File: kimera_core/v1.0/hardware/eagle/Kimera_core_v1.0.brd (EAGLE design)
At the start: 26 x 12 mm, 24 parts, among them IC1 PCA9555RGER-NOPAD, IC2 PCA9555RGER-NOPAD, U1 ATMEGA32U4QFN2, Y1 CSTCR6M00G53Z

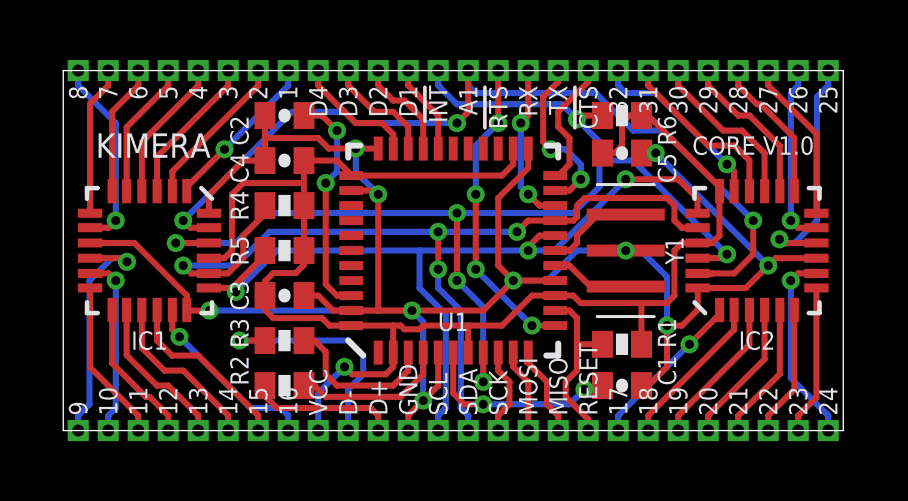
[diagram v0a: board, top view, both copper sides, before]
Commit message: kimera_core: Change signal name of LED pins
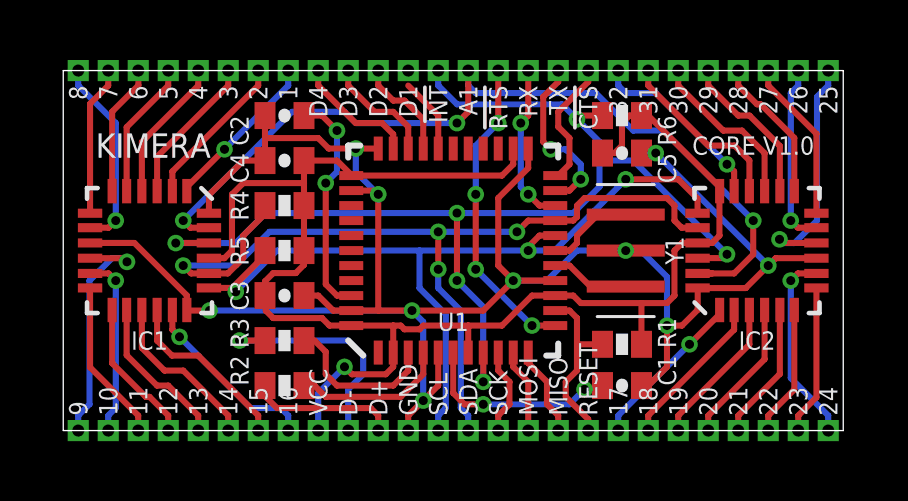
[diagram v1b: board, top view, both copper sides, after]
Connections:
- net L1 renamed LED1
- net L2 renamed LED2
- net L3 renamed LED3
- net L4 renamed LED4
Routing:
- net LED1: track 3.01 -> 2.51 mm
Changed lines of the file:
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@@
 <param name="rlMinPadBottom" value="6mil"/>
 <param name="rlMaxPadBottom" value="20mil"/>
-<param name="rlMinViaOuter" value="6mil"/>
+<param name="rlMinViaOuter" value="5mil"/>
 <param name="rlMaxViaOuter" value="20mil"/>
 <param name="rlMinViaInner" value="6mil"/>
@@
 <wire x1="14.5" y1="10.25" x2="14.5" y2="12" width="0.2032" layer="1"/>
 </signal>
-<signal name="L2">
+<signal name="LED2">
 <contactref element="JP6" pad="8"/>
 <contactref element="U1" pad="30"/>
@@
 <wire x1="10.5" y1="11.5" x2="10.5" y2="12" width="0.2032" layer="1"/>
 </signal>
-<signal name="L1">
-<contactref element="JP6" pad="7"/>
-<contactref element="U1" pad="29"/>
-<wire x1="12.5" y1="9.4" x2="12.5" y2="10.5" width="0.2032" layer="1"/>
-<wire x1="12.5" y1="10.5" x2="11.5" y2="11.5" width="0.2032" layer="1"/>
-<wire x1="11.5" y1="11.5" x2="11.5" y2="12" width="0.2032" layer="1"/>
-</signal>
-<signal name="L3">
+<signal name="LED3">
 <contactref element="JP6" pad="9"/>
 <contactref element="U1" pad="31"/>
@@
 <wire x1="9.5" y1="11.5" x2="9.5" y2="12" width="0.2032" layer="1"/>
 </signal>
-<signal name="L4">
+<signal name="LED4">
 <contactref element="JP6" pad="10"/>
 <contactref element="U1" pad="32"/>
@@
 <wire x1="17.5" y1="11.625" x2="17.5" y2="12" width="0.2032" layer="1"/>
 </signal>
+<signal name="LED1">
+<contactref element="JP6" pad="7"/>
+<contactref element="U1" pad="29"/>
+<wire x1="12.5" y1="9.4" x2="12.5" y2="10.5" width="0.2032" layer="1"/>
+<wire x1="12.5" y1="10.5" x2="11.5" y2="11.5" width="0.2032" layer="1"/>
+<wire x1="11.5" y1="11.5" x2="11.5" y2="12" width="0" layer="19" extent="1-1"/>
+</signal>
 </signals>
